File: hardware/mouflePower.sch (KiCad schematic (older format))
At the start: 42 parts, among them J1 FTDI, J10 EINK, J11 ANALOG, J2 Antenna, J3 I2C, J4 ICSP, J5 V_MAIN, J6 Relay, J7 SPI, J8 I2C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

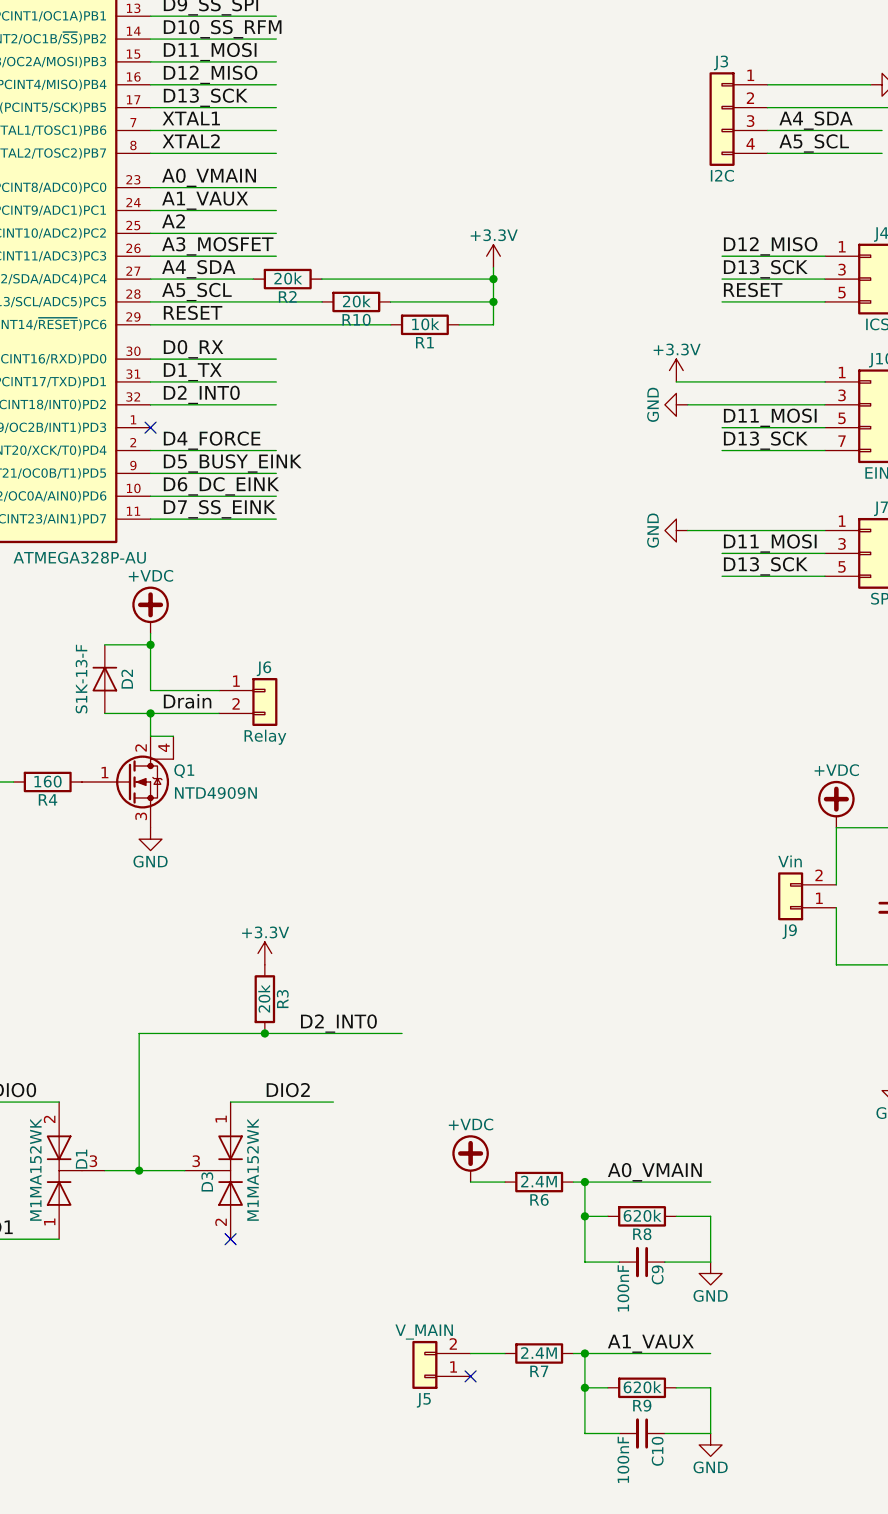
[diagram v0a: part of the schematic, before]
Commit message: ADC pin naming correction
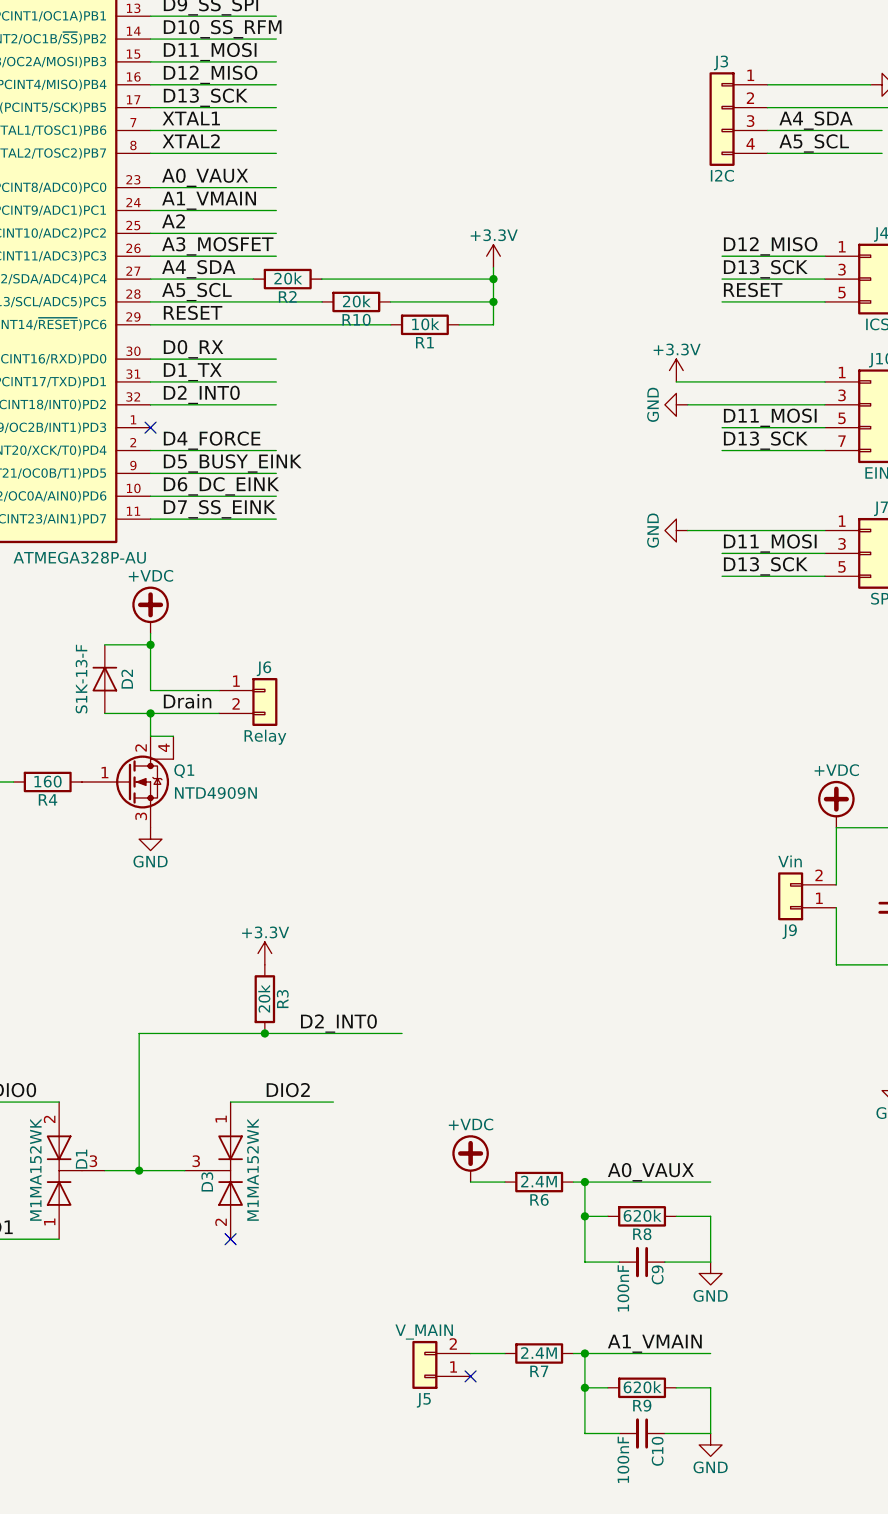
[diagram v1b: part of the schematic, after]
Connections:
- net labels added: A0_VAUX, A1_VMAIN
- net labels removed: A0_VMAIN, A1_VAUX
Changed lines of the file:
@@
 	3900 1950 4450 1950
 Text Label 3950 1950 0    60   ~ 0
-A0_VMAIN
+A0_VAUX
 Wire Wire Line
 	5800 6300 5800 6650
@@
 	5800 6450 5900 6450
 Text Label 5900 6300 0    60   ~ 0
-A0_VMAIN
+A0_VAUX
 $Comp
 L R R9
@@
 	5800 7200 5900 7200
 Text Label 5900 7050 0    60   ~ 0
-A1_VAUX
+A1_VMAIN
 Text Label 3950 2050 0    60   ~ 0
-A1_VAUX
+A1_VMAIN
 Wire Wire Line
 	3900 2050 4450 2050
